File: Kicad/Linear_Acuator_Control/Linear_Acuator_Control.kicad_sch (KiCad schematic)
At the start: 6 parts, among them K1 DPDT Relay, K2 DPDT Relay, K3 SPST Relay, K4 SPST Relay

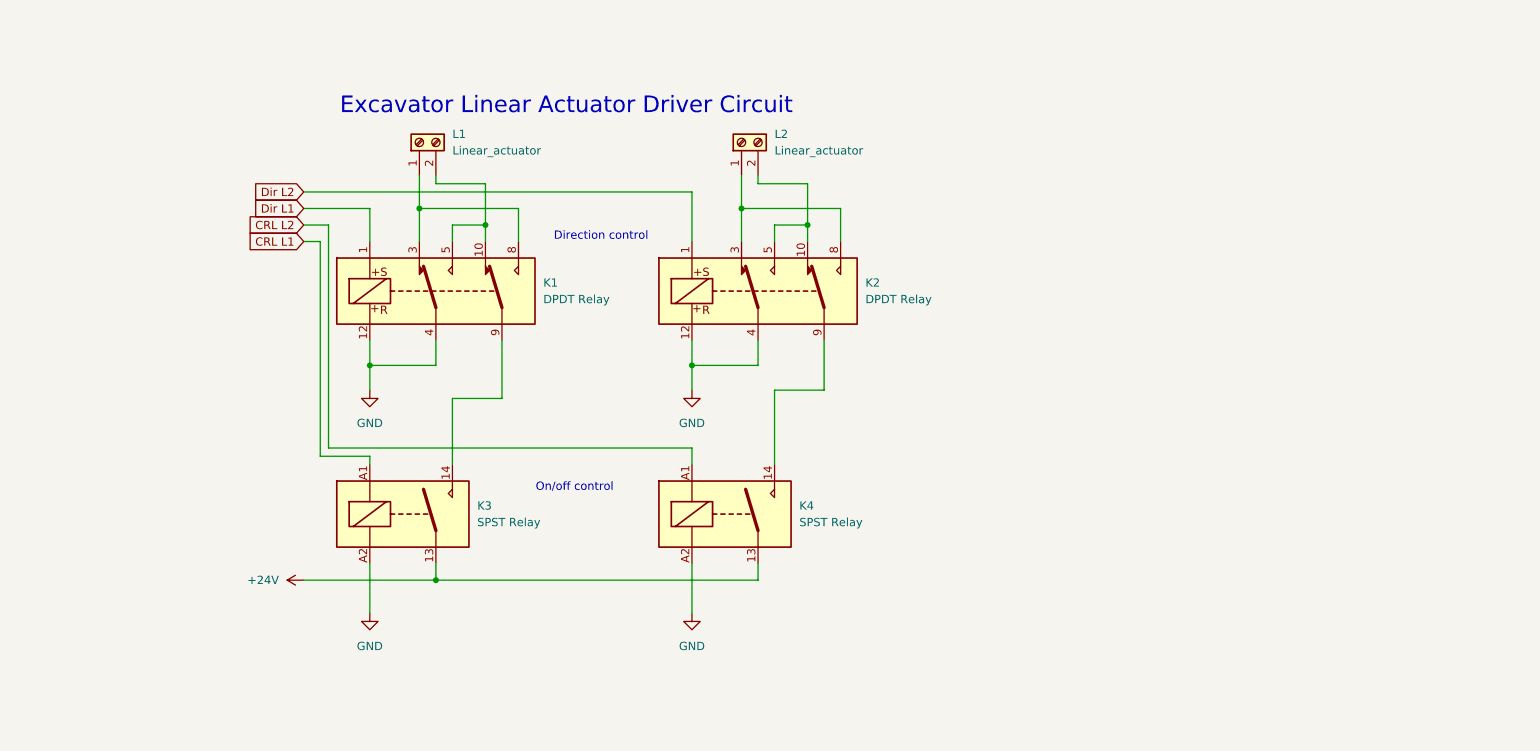
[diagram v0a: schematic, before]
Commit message: commit updated schematic
shifted to solid state control for motor speed, with relays for direction, need to discuss relay selection to ensure adequate current carrying capacity.
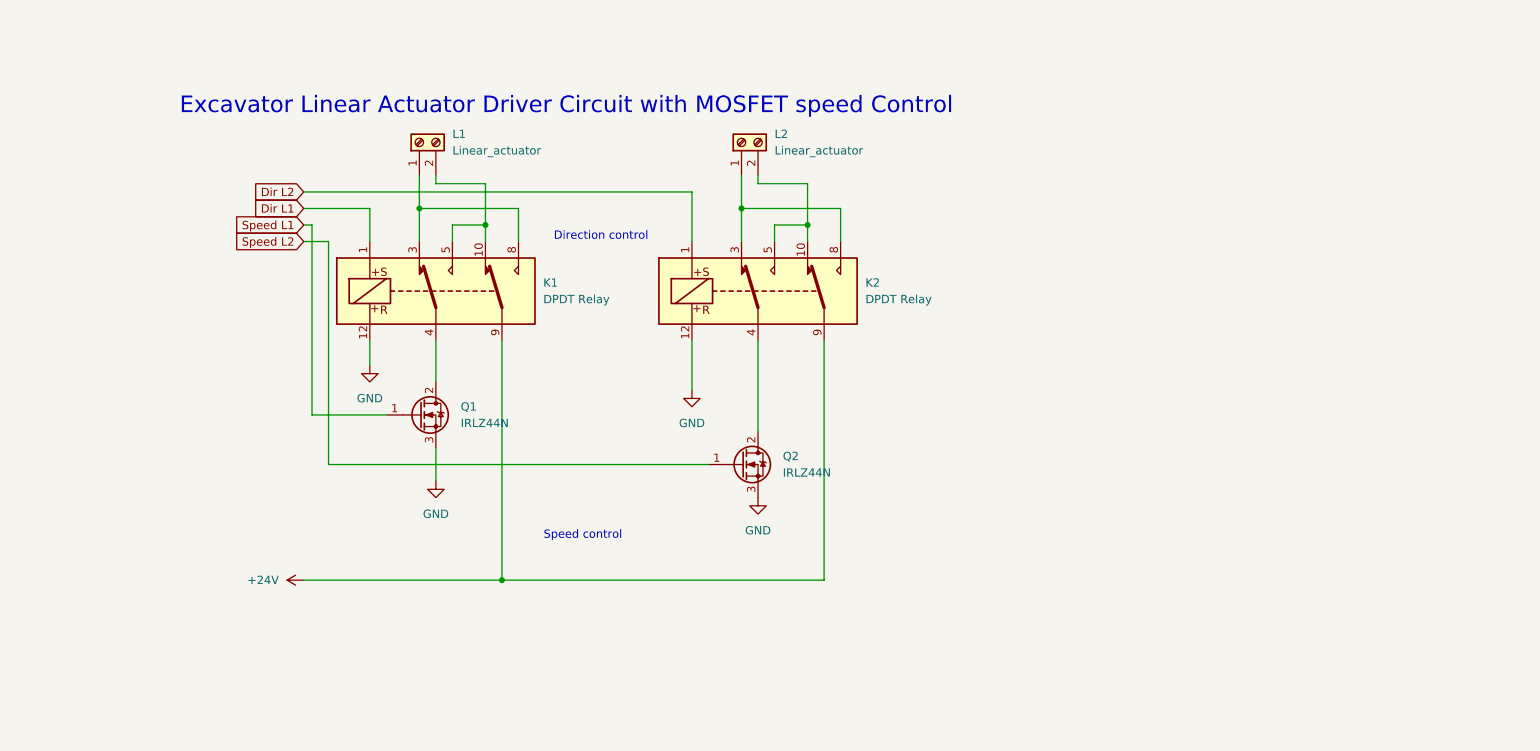
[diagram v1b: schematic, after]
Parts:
- removed K3, K4: SPST Relay, Relay_THT:Relay_SPST-NO_Fujitsu_FTR-LYAA005x_FormA_Vertical, symbol Relay:Fujitsu_FTR-LYAA005x
- added Q1, Q2: IRLZ44N, Package_TO_SOT_THT:TO-220-3_Vertical, symbol Transistor_FET:IRLZ44N
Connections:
- net +24V: now also K1.9, K2.9
- net GND: now also Q1.3 (S), Q2.3 (S); no longer K1.4, K2.4
- new net: K2.4, Q2.2 (D)
- new net: K1.4, Q1.2 (D)
- new net Speed L1: Q1.1 (G)
- new net Speed L2: Q2.1 (G)
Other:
- note added: "Excavator Linear Actuator Driver Circuit with MOSFET speed Control"
- note added: "Speed control"
- note removed: "Excavator Linear Actuator Driver Circuit"
- note removed: "On/off control"

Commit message: flyback diode for protections
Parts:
- added D1, D2: MBR745, Package_TO_SOT_THT:TO-220-2_Vertical, symbol Diode:MBR745
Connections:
- net +24V: now also D1.1 (K), D2.1 (K)
- net at K2.4, Q2.2 (D): now also D2.2 (A)
- net at K1.4, Q1.2 (D): now also D1.2 (A)
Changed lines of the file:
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@@
+	)
+	(junction
+		(at 170.18 104.14)
+		(diameter 0)
+		(color 0 0 0 0)
+	)
+	(junction
+		(at 120.65 96.52)
+		(diameter 0)
+		(color 0 0 0 0)
 	)
 	(junction
@@
 	)
 	(junction
+		(at 130.81 96.52)
+		(diameter 0)
+		(color 0 0 0 0)
+	)
+	(junction
 		(at 177.8 72.39)
 		(diameter 0)
@@
 		(color 0 0 0 0)
 	)
+	(junction
+		(at 180.34 104.14)
+		(diameter 0)
+		(color 0 0 0 0)
+	)
 	(wire
 		(pts
@@
 	(wire
 		(pts
+			(xy 130.81 96.52) (xy 130.81 127)
+		)
+		(stroke
+			(width 0)
+			(type default)
+		)
+	)
+	(wire
+		(pts
 			(xy 118.11 64.77) (xy 118.11 69.85)
 		)
@@
 	(wire
 		(pts
+			(xy 172.72 104.14) (xy 170.18 104.14)
+		)
+		(stroke
+			(width 0)
+			(type default)
+		)
+	)
+	(wire
+		(pts
 			(xy 120.65 106.68) (xy 120.65 111.76)
 		)
@@
 	(wire
 		(pts
+			(xy 128.27 96.52) (xy 130.81 96.52)
+		)
+		(stroke
+			(width 0)
+			(type default)
+		)
+	)
+	(wire
+		(pts
 			(xy 120.65 66.04) (xy 128.27 66.04)
 		)
@@
 	(wire
 		(pts
-			(xy 130.81 90.17) (xy 130.81 127)
+			(xy 130.81 90.17) (xy 130.81 96.52)
 		)
 		(stroke
@@
 	(wire
 		(pts
+			(xy 180.34 104.14) (xy 180.34 127)
+		)
+		(stroke
+			(width 0)
+			(type default)
+		)
+	)
+	(wire
+		(pts
 			(xy 104.14 109.22) (xy 162.56 109.22)
 		)
@@
 	(wire
 		(pts
-			(xy 180.34 90.17) (xy 180.34 127)
+			(xy 180.34 90.17) (xy 180.34 104.14)
 		)
 		(stroke
@@
 	)
 	(symbol
+		(lib_id "Diode:MBR745")
+		(at 176.53 104.14 180)
+		(unit 1)
+		(exclude_from_sim no)
+		(in_bom yes)
+		(on_board yes)
+		(dnp no)
+		(fields_autoplaced yes)
+		(property "Reference" "D2"
+			(at 176.8475 97.79 0)
+			(effects
+				(font
+					(size 1.27 1.27)
+				)
+			)
+		)
+		(property "Value" "MBR745"
+			(at 176.8475 100.33 0)
+			(effects
+				(font
+					(size 1.27 1.27)
+				)
+			)
+		)
+		(property "Footprint" "Package_TO_SOT_THT:TO-220-2_Vertical"
+			(at 176.53 99.695 0)
+			(effects
+				(font
+					(size 1.27 1.27)
+				)
+				(hide yes)
+			)
+		)
+		(property "Datasheet" "http://www.onsemi.com/pub_link/Collateral/MBR735-D.PDF"
+			(at 176.53 104.14 0)
+			(effects
+				(font
+					(size 1.27 1.27)
+				)
+				(hide yes)
+			)
+		)
+		(property "Description" "45V 7.5A Schottky Barrier Rectifier Diode, TO-220"
+			(at 176.53 104.14 0)
+			(effects
+				(font
+					(size 1.27 1.27)
+				)
+				(hide yes)
+			)
+		)
+		(pin "1"
+		)
+		(pin "2"
+		)
+		(instances
+			(project "Linear_Acuator_Control"
+				(path "/f7047aaa-ba32-49d1-99b3-f492bbec601f"
+					(reference "D2")
+					(unit 1)
+				)
+			)
+		)
+	)
+	(symbol
 		(lib_id "power:GND")
 		(at 110.49 93.98 0)
@@
 					(unit 1)
 				)
+			)
+		)
+	)
+	(symbol
+		(lib_id "Diode:MBR745")
+		(at 124.46 96.52 180)
+		(unit 1)
+		(exclude_from_sim no)
+		(in_bom yes)
+		(on_board yes)
+		(dnp no)
+		(fields_autoplaced yes)
+		(property "Reference" "D1"
+			(at 124.7775 90.17 0)
+			(effects
+				(font
+					(size 1.27 1.27)
+				)
+			)
+		)
+		(property "Value" "MBR745"
+			(at 124.7775 92.71 0)
+			(effects
+				(font
+					(size 1.27 1.27)
+				)
+			)
+		)
+		(property "Footprint" "Package_TO_SOT_THT:TO-220-2_Vertical"
+			(at 124.46 92.075 0)
+			(effects
+				(font
+					(size 1.27 1.27)
+				)
+				(hide yes)
+			)
+		)
+		(property "Datasheet" "http://www.onsemi.com/pub_link/Collateral/MBR735-D.PDF"
+			(at 124.46 96.52 0)
+			(effects
+				(font
+					(size 1.27 1.27)
+				)
+				(hide yes)
+			)
+		)
+		(property "Description" "45V 7.5A Schottky Barrier Rectifier Diode, TO-220"
+			(at 124.46 96.52 0)
+			(effects
+				(font
+					(size 1.27 1.27)
+				)
+				(hide yes)
+			)
+		)
+		(pin "1"
+		)
+		(pin "2"
+		)
+		(instances
+			(project "Linear_Acuator_Control"
+				(path "/f7047aaa-ba32-49d1-99b3-f492bbec601f"
+					(reference "D1")
+					(unit 1)
+				)

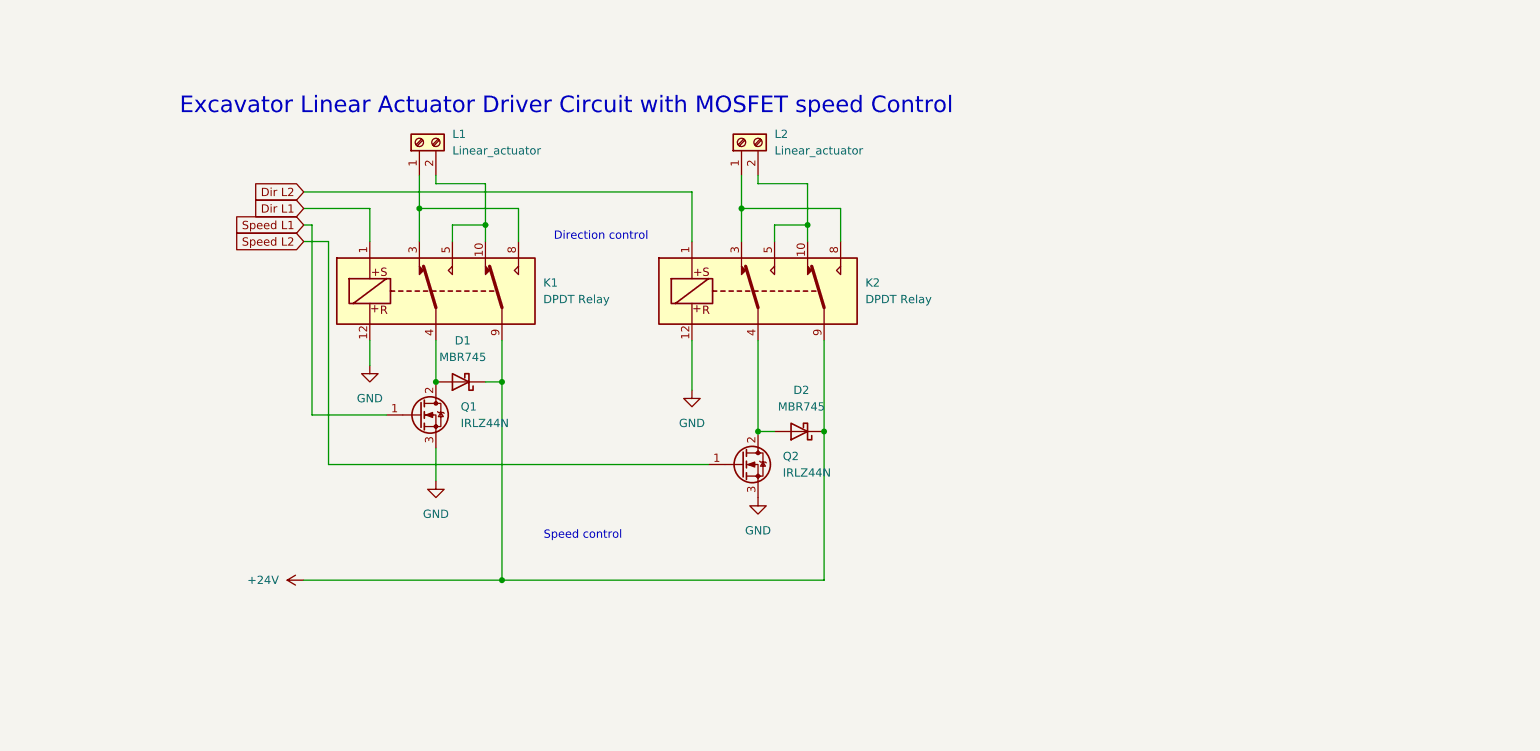
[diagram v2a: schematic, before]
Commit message: Modified schematic for ESP32 integration and routed PCB
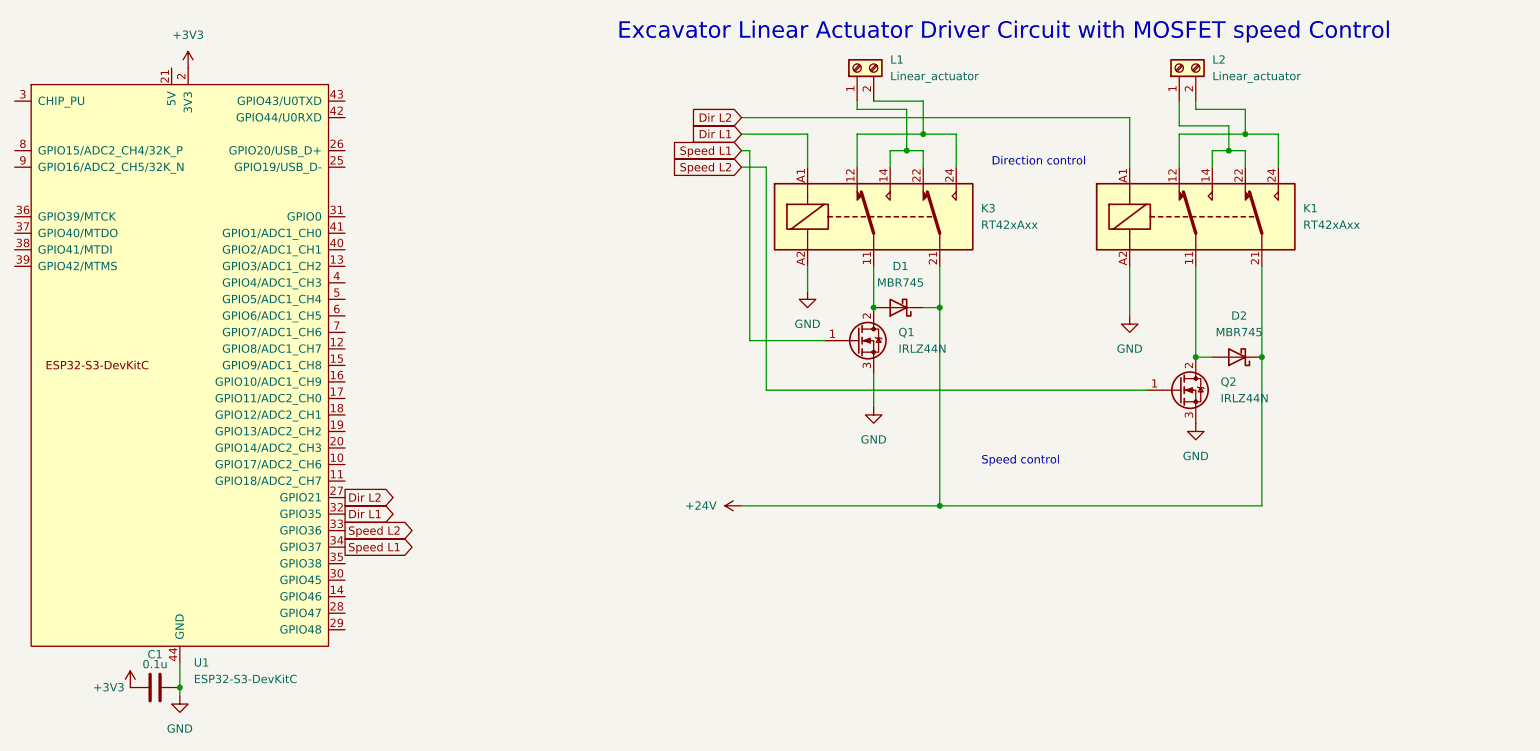
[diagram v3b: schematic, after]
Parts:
- removed K1, K2: DPDT Relay, Relay_SMD:Relay_DPDT_Kemet_EE2_NU, symbol Relay:EE2-12SNU
- added C1: 0.1u, Capacitor_SMD:C_0603_1608Metric, symbol Device:C
- added K1, K3: RT42xAxx, Relay_THT:Relay_DPDT_Schrack-RT2-FormC_RM5mm, symbol Relay:RT42xAxx
- added U1: ESP32-S3-DevKitC, PCM_Espressif:ESP32-S3-DevKitC, symbol PCM_Espressif:ESP32-S3-DevKitC
- L1, L2: footprint (none) -> Connector_AMASS:AMASS_XT60PW-F_1x02_P7.20mm_Horizontal
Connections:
- net +24V: now also K1.21, K3.21
- net Dir L1: now also K3.A1, U1.32 (GPIO35)
- net Dir L2: now also K1.A1, U1.27 (GPIO21)
- net GND: now also C1.1, K1.A2, K3.A2, U1.22 (GND), U1.23 (GND), U1.24 (GND), U1.44 (GND)
- net Speed L1: now also U1.34 (GPIO37)
- net Speed L2: now also U1.33 (GPIO36)
- net at L2.2 (Pin_2): now also K1.12, K1.24
- net at L2.1 (Pin_1): now also K1.14, K1.22
- net at D2.2 (A), Q2.2 (D): now also K1.11
- net at L1.2 (Pin_2): now also K3.12, K3.24
- net at L1.1 (Pin_1): now also K3.14, K3.22
- net at D1.2 (A), Q1.2 (D): now also K3.11
- new net +3V3: C1.2, U1.1 (3V3), U1.2 (3V3)
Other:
- moved on the sheet: D1, D2, L1, L2, Q1, Q2
